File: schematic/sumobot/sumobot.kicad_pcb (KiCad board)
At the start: 2 copper layers, 80 x 30 mm, 6 parts, among them J1 Screw_Terminal_01x02, J2 Screw_Terminal_01x02, J3 Screw_Terminal_01x02, J4 Conn_01x05, U1 ROB-14450

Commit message: fix: update net names and add junctions in schematic and PCB for improved connectivity
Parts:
- added J5: Screw_Terminal_01x02, TerminalBlock:TerminalBlock_MaiXu_MX126-5.0-02P_1x02_P5.00mm, F.Cu at (147.3, 91.3)
- added J6: Screw_Terminal_01x02, TerminalBlock:TerminalBlock_MaiXu_MX126-5.0-02P_1x02_P5.00mm, F.Cu at (147.3, 101.4)
- added J7: Conn_01x05, Connector_PinHeader_1.00mm:PinHeader_1x05_P1.00mm_Vertical, F.Cu at (145.0, 108.0)
- added U2: ROB-14450, TB6612FNG:MODULE_ROB-14450, F.Cu at (132.4, 97.7)
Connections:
- A1 pad 19: Net-(A1-A0) -> unconnected-(A1-A0-Pad19)
- A1 pad 20: Net-(A1-A1) -> unconnected-(A1-A1-Pad20)
- A1 pad 21: Net-(A1-A2) -> unconnected-(A1-A2-Pad21)
- A1 pad 22: Net-(A1-A3) -> unconnected-(A1-A3-Pad22)
- A1 pad 24: unconnected-(A1-A5-Pad24) -> Net-(A1-A5)
- A1 pad 27: Net-(A1-+5V) -> +BATT
- A1 pad 29: unconnected-(A1-GND-Pad29) -> Net-(J4-Pin_2)
- A1 pad 6: unconnected-(A1-D3-Pad6) -> Net-(A1-A4)
- A1 pad 7: unconnected-(A1-D4-Pad7) -> Net-(A1-D4)
- J1 pad 1: Net-(J1-Pin_1) -> +BATT
- J1 pad 2: Net-(J1-Pin_2) -> +BATT
- J2 pad 1: Net-(J2-Pin_1) -> +BATT
- J2 pad 2: Net-(J2-Pin_2) -> +BATT
- J3 pad 2: -BATT -> +BATT
- J4 pad 1: Net-(A1-A0) -> +BATT
- J4 pad 2: Net-(A1-A1) -> Net-(J4-Pin_2)
- J4 pad 3: Net-(A1-A2) -> Net-(A1-A5)
- J4 pad 4: Net-(A1-A3) -> Net-(A1-A4)
- U1 pad 13: Net-(A1-+5V) -> +BATT
- U1 pad 2: Net-(A1-+5V) -> +BATT
- U1 pad 3: -BATT -> +BATT
- U1 pad 4: Net-(J1-Pin_1) -> +BATT
- U1 pad 5: Net-(J1-Pin_2) -> +BATT
- U1 pad 6: Net-(J2-Pin_2) -> +BATT
- U1 pad 7: Net-(J2-Pin_1) -> +BATT
- U1 pad 8: -BATT -> +BATT
- U1 pad 9: -BATT -> +BATT

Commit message: haha
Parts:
- removed A1: Arduino_Nano_v2.x, Module:Arduino_Nano
- removed J1, J2, J3, J5, J6: Screw_Terminal_01x02, TerminalBlock:TerminalBlock_MaiXu_MX126-5.0-02P_1x02_P5.00mm
- removed J4, J7: Conn_01x05, Connector_PinHeader_1.00mm:PinHeader_1x05_P1.00mm_Vertical
- removed U1, U2: ROB-14450, TB6612FNG:MODULE_ROB-14450

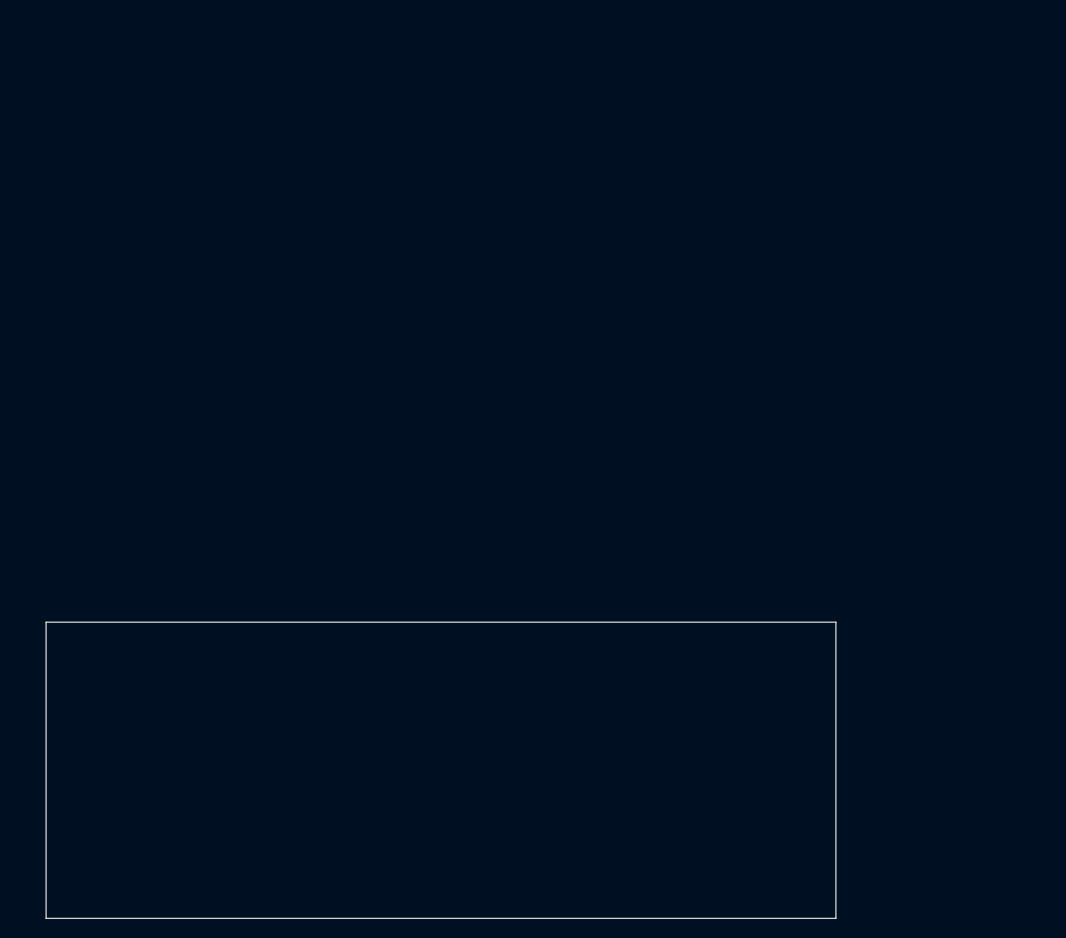
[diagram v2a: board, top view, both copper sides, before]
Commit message: feat: add new 3D models and schematic
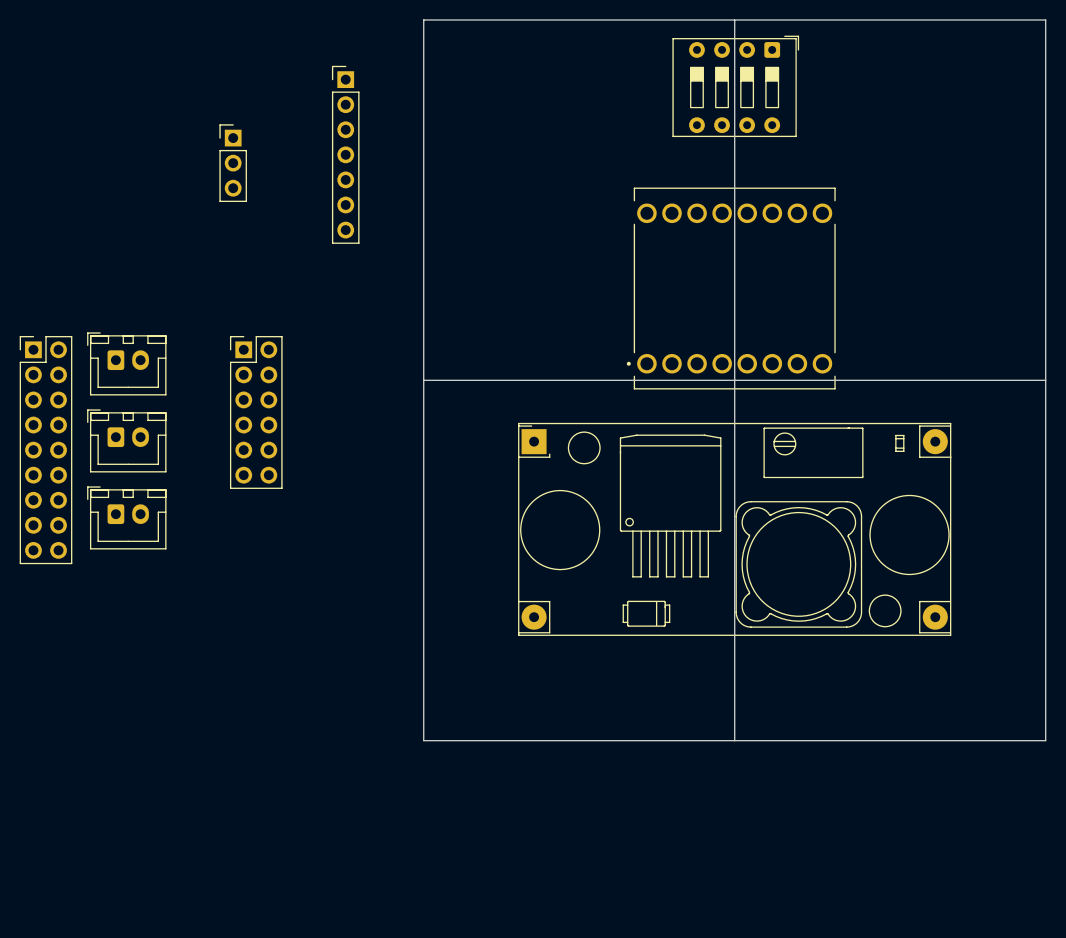
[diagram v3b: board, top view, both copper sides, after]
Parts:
- added J1: Conn_02x09_Odd_Even, Connector_PinHeader_2.54mm:PinHeader_2x09_P2.54mm_Vertical, F.Cu at (65.5, 95.4)
- added J2: Conn_01x03, Connector_PinHeader_2.54mm:PinHeader_1x03_P2.54mm_Vertical, F.Cu at (85.7, 74.0)
- added J3: Conn_02x06_Counter_Clockwise, Connector_PinHeader_2.54mm:PinHeader_2x06_P2.54mm_Vertical, F.Cu at (86.8, 95.4)
- added J4: Conn_01x02_Socket, Connector_JST:JST_XH_B2B-XH-A_1x02_P2.50mm_Vertical, F.Cu at (73.8, 96.5)
- added J5: Conn_01x02_Socket, Connector_JST:JST_XH_B2B-XH-A_1x02_P2.50mm_Vertical, F.Cu at (73.8, 104.3)
- added J6: Conn_01x02_Socket, Connector_JST:JST_XH_B2B-XH-A_1x02_P2.50mm_Vertical, F.Cu at (73.8, 112.1)
- added J7: Conn_01x07, Connector_PinHeader_2.54mm:PinHeader_1x07_P2.54mm_Vertical, F.Cu at (97.1, 68.0)
- added SW3: SW_DIP_x04, Button_Switch_THT:SW_DIP_SPSTx04_Slide_9.78x12.34mm_W7.62mm_P2.54mm, F.Cu at (140.3, 65.0)
- added U1: ROB-14450, TB6612FNG:MODULE_ROB-14450, F.Cu at (136.5, 89.2)
- added U2: YAAJ_DCDC_StepDown_LM2596, LM2596-Buck-Converter:YAAJ_DCDC_StepDown_LM2596, F.Cu at (116.2, 104.7)
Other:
- board size 80 x 30 mm -> 63 x 73 mm
